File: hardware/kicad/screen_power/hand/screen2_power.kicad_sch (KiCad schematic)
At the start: 16 parts, among them J203 EVM 5V, J204 EVM CONTROL, K202 G5LE-1 DC5, Q201 2N7000, Q202 2N3906, Q203 IRLZ44NPBF

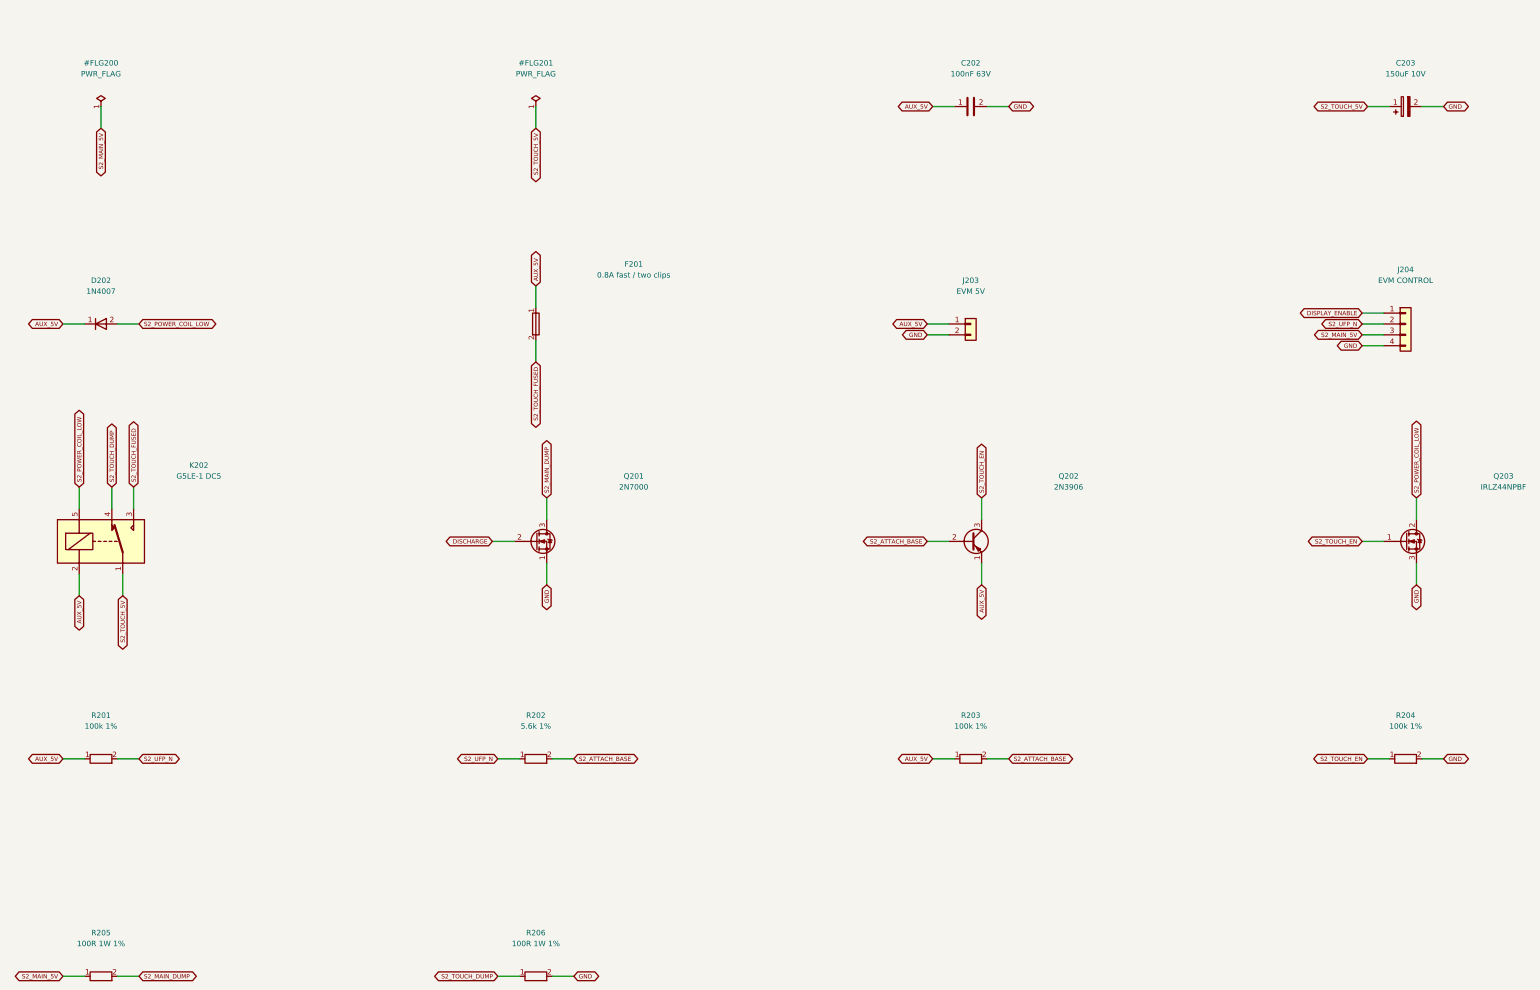
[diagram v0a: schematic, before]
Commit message: refactor(hardware): simplify and compact screen power boards
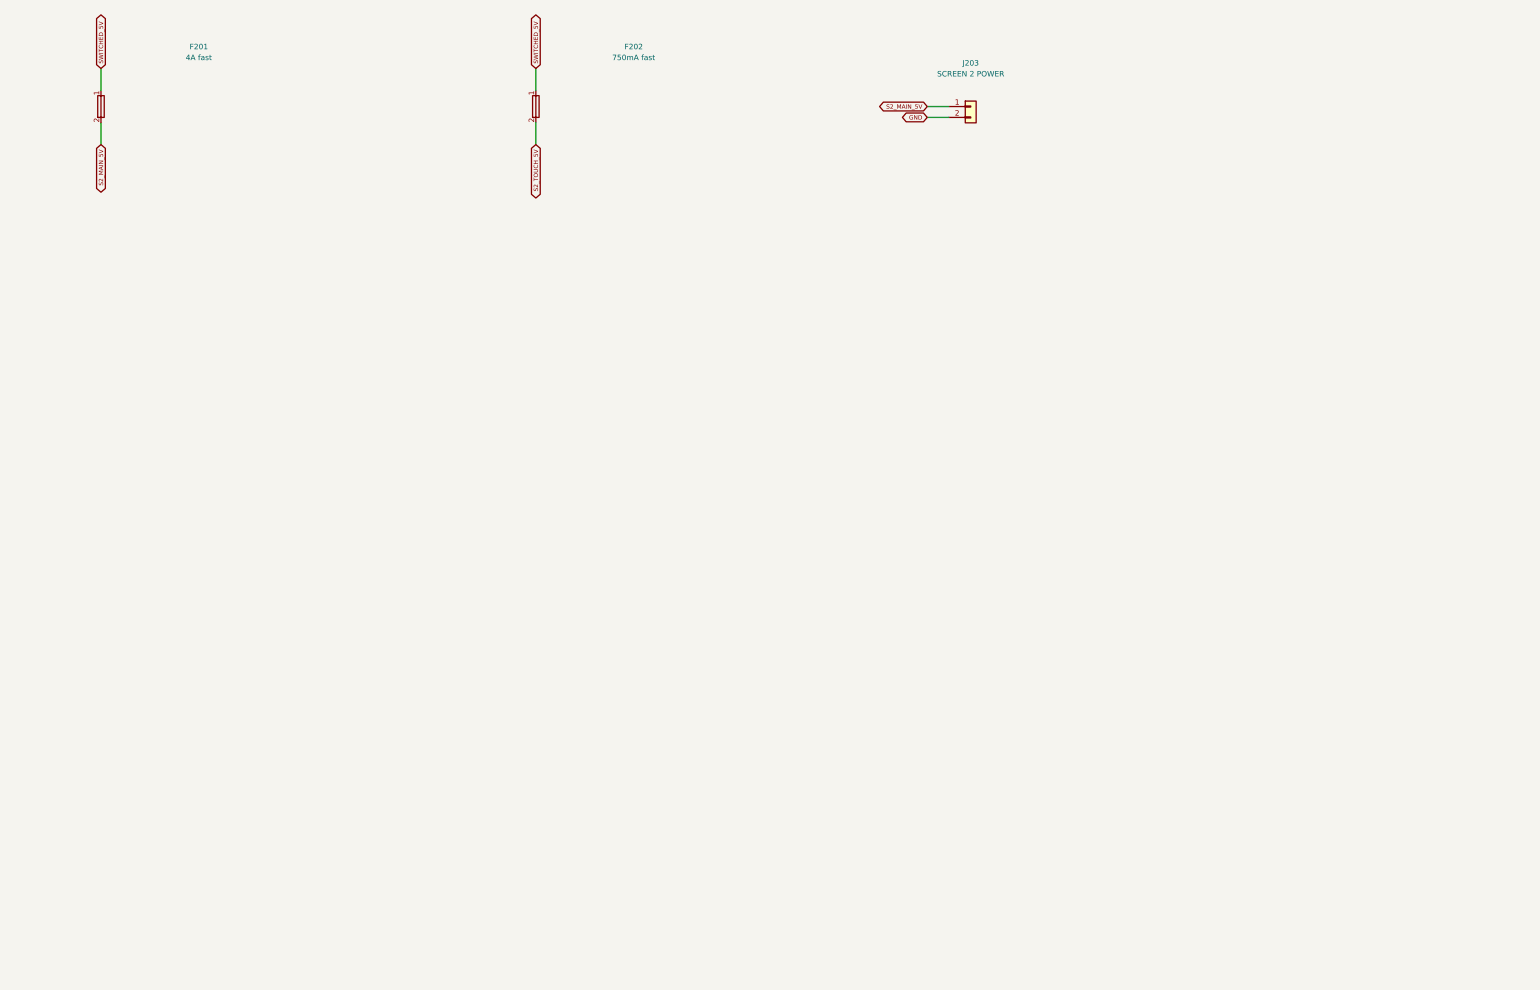
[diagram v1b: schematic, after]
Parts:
- removed C202: 100nF 63V, Capacitor_THT:C_Rect_L7.2mm_W2.5mm_P5.00mm, symbol screen_symbols:Device_C
- removed C203: 150uF 10V, Capacitor_THT:CP_Radial_D5.0mm_P2.00mm, symbol screen_symbols:Device_C_Polarized
- removed D202: 1N4007, Diode_THT:D_DO-41_SOD81_P10.16mm_Horizontal, symbol screen_symbols:Diode_1N4007
- removed J204: EVM CONTROL, Connector_JST:JST_XH_B4B-XH-A_1x04_P2.50mm_Vertical, symbol screen_symbols:Connector_Generic_Conn_01x04
- removed K202: G5LE-1 DC5, Relay_THT:Relay_SPDT_Omron-G5LE-1, symbol screen_symbols:Relay_G5LE-1
- removed Q201: 2N7000, Package_TO_SOT_THT:TO-92_Inline_Wide, symbol screen_symbols:Transistor_FET_2N7000
- removed Q202: 2N3906, Package_TO_SOT_THT:TO-92_Inline_Wide, symbol screen_symbols:Transistor_BJT_2N3906
- removed Q203: IRLZ44NPBF, Package_TO_SOT_THT:TO-220-3_Vertical, symbol screen_symbols:Transistor_FET_IRLZ44N
- removed R201, R203, R204: 100k 1%, Resistor_THT:R_Axial_DIN0207_L6.3mm_D2.5mm_P10.16mm_Horizontal, symbol screen_symbols:Device_R
- removed R202: 5.6k 1%, Resistor_THT:R_Axial_DIN0207_L6.3mm_D2.5mm_P10.16mm_Horizontal, symbol screen_symbols:Device_R
- removed R205, R206: 100R 1W 1%, Resistor_THT:R_Axial_DIN0207_L6.3mm_D2.5mm_P10.16mm_Horizontal, symbol screen_symbols:Device_R
- added F202: 750mA fast, screen_power:Fuse_Littelfuse_251_P12.70mm, symbol screen_symbols:Device_Fuse
- F201: value 0.8A fast / two clips -> 4A fast; footprint Fuse:Fuseholder_Clip-5x20mm_Littelfuse_111_Lateral_P18.80x5.00mm_D1.17mm_Horizontal -> screen_power:Fuse_Littelfuse_251_P12.70mm; MPN 01110501Z -> 0251004.MXL
- J203: value EVM 5V -> SCREEN 2 POWER
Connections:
- net S2_TOUCH_FUSED is gone; now on net S2_MAIN_5V: F201.2
- net S2_MAIN_5V: now also J203.1 (Pin_1)
- net S2_TOUCH_5V: now also F202.2
- net AUX_5V renamed SWITCHED_5V
- net SWITCHED_5V: now also F202.1; no longer J203.1 (Pin_1)
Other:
- moved on the sheet: F201, J203

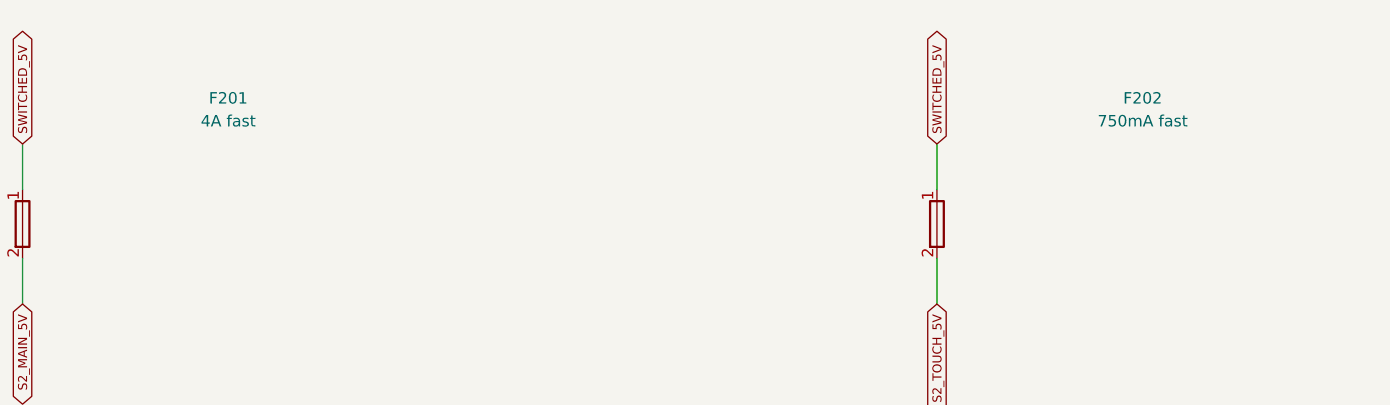
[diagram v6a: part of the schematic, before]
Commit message: feat(hardware): lower screen power cost and finish copper contours
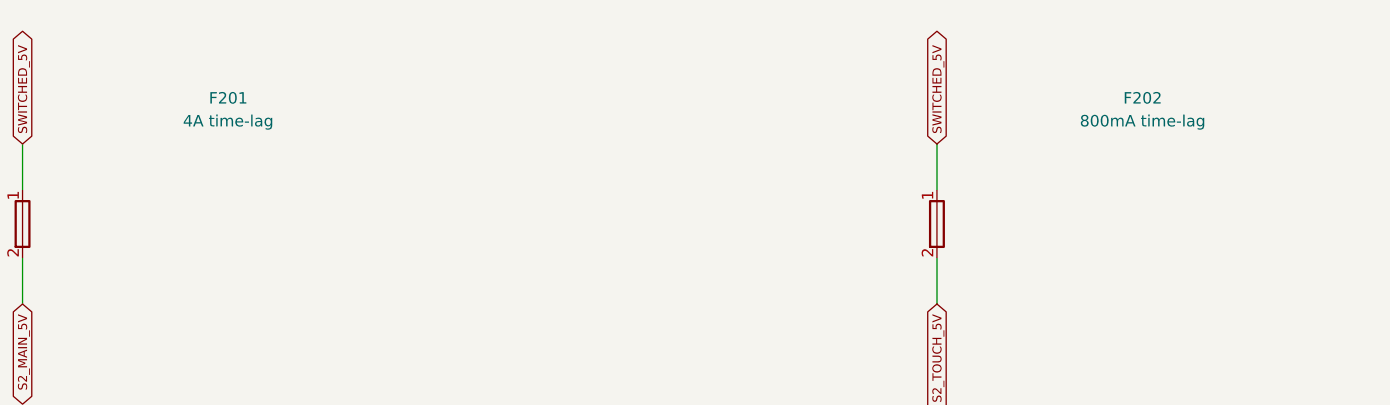
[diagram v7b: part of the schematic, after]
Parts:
- F201: value 4A fast -> 4A time-lag; footprint screen_power:Fuse_Littelfuse_251_P12.70mm -> screen_power:Fuse_Bel_0697H_P5.08mm; MPN 0251004.MXL -> 0697H4000-02
- F202: value 750mA fast -> 800mA time-lag; footprint screen_power:Fuse_Littelfuse_251_P12.70mm -> screen_power:Fuse_Bel_0697H_P5.08mm; MPN 0251.750MXL -> 0697H0800-02
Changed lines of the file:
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@@
   (title_block
     (title "Segno screen power / hand / screen2 power")
-    (rev "M prototype")
-    (comment 1 "AUX-powered relays; each host VBUS supplies only its presence detector.")
-    (comment 2 "Physical verification required before release."))
+    (rev "N prototype")
+    (comment 1 "One normally open contact switches AUX; every board load sits behind F1.")
+    (comment 2 "AUX-powered relays; each host VBUS supplies only its presence detector.")
+    (comment 3 "Physical verification required before release."))
   (wire
     (pts
@@
         (font
           (size 1.27 1.27))))
-    (property "Value" "4A fast"
+    (property "Value" "4A time-lag"
       (at 73.66 52.07 0)
       (effects
         (font
           (size 1.27 1.27))))
-    (property "Footprint" "screen_power:Fuse_Littelfuse_251_P12.70mm"
+    (property "Footprint" "screen_power:Fuse_Bel_0697H_P5.08mm"
       (at 73.66 63.5 0)
       (effects
@@
           (size 1.27 1.27))
         (hide yes)))
-    (property "MPN" "0251004.MXL"
+    (property "MPN" "0697H4000-02"
       (at 73.66 63.5 0)
       (effects
@@
         (font
           (size 1.27 1.27))))
-    (property "Value" "750mA fast"
+    (property "Value" "800mA time-lag"
       (at 175.26 52.07 0)
       (effects
         (font
           (size 1.27 1.27))))
-    (property "Footprint" "screen_power:Fuse_Littelfuse_251_P12.70mm"
+    (property "Footprint" "screen_power:Fuse_Bel_0697H_P5.08mm"
       (at 175.26 63.5 0)
       (effects
@@
           (size 1.27 1.27))
         (hide yes)))
-    (property "MPN" "0251.750MXL"
+    (property "MPN" "0697H0800-02"
       (at 175.26 63.5 0)
       (effects
